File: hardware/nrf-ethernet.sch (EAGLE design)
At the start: 71 parts, among them J2 J0026, J3 RJ45-8PTH, U1 KSZ8081RNA, U2 NRF24L01SMD, U4 MIC5301, U5 MAX3051, U6 STM32F107XX, Y1 8MHz, Y2 16M, Y3 25MHz

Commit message: value update
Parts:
- C29, C30: value 16p -> 18p
- R36: value 120 -> 100k
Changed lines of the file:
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@@
 <part name="GND41" library="supply1" deviceset="GND" device=""/>
 <part name="GND42" library="supply1" deviceset="GND" device=""/>
-<part name="R36" library="rcl" deviceset="R-EU_" device="R0603" value="120"/>
+<part name="R36" library="rcl" deviceset="R-EU_" device="R0603" value="100k"/>
 <part name="GND43" library="supply1" deviceset="GND" device=""/>
 <part name="C34" library="rcl" deviceset="C-EU" device="C0603" value="100n"/>
@@
 <part name="P+9" library="supply1" deviceset="VCC" device=""/>
 <part name="P+12" library="supply1" deviceset="VCC" device=""/>
-<part name="C29" library="rcl" deviceset="C-EU" device="C0603" value="16p"/>
-<part name="C30" library="rcl" deviceset="C-EU" device="C0603" value="16p"/>
+<part name="C29" library="rcl" deviceset="C-EU" device="C0603" value="18p"/>
+<part name="C30" library="rcl" deviceset="C-EU" device="C0603" value="18p"/>
 <part name="C6" library="rcl" deviceset="C-EU" device="C0603" value=".1u"/>
 <part name="C17" library="rcl" deviceset="C-EU" device="C0603" value=".1u"/>

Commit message: hw: fix some part number value
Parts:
- C29, C30: value 18p -> 33p
- Y1: value 8MHz -> 25MHz
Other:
- note removed: "Alternative: 25MHz"
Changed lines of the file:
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@@
 <part name="LED3" library="led" deviceset="LED" device="CHIPLED_0805"/>
 <part name="S3" library="sparkfun" deviceset="SWITCH-MOMENTARY-2" device="SMD" value="SWITCH"/>
-<part name="Y1" library="sparkfun" deviceset="CRYSTAL" device="5X3" value="8MHz"/>
+<part name="Y1" library="sparkfun" deviceset="CRYSTAL" device="5X3" value="25MHz"/>
 <part name="GND6" library="supply1" deviceset="GND" device=""/>
 <part name="GND7" library="supply1" deviceset="GND" device=""/>
@@
 <part name="P+9" library="supply1" deviceset="VCC" device=""/>
 <part name="P+12" library="supply1" deviceset="VCC" device=""/>
-<part name="C29" library="rcl" deviceset="C-EU" device="C0603" value="18p"/>
-<part name="C30" library="rcl" deviceset="C-EU" device="C0603" value="18p"/>
+<part name="C29" library="rcl" deviceset="C-EU" device="C0603" value="33p"/>
+<part name="C30" library="rcl" deviceset="C-EU" device="C0603" value="33p"/>
 <part name="C6" library="rcl" deviceset="C-EU" device="C0603" value=".1u"/>
 <part name="C17" library="rcl" deviceset="C-EU" device="C0603" value=".1u"/>
@@
 <text x="96.52" y="134.62" size="1.778" layer="97">GPIO</text>
 <text x="15.24" y="149.86" size="1.778" layer="97" rot="MR0">GPIO</text>
-<text x="111.76" y="106.68" size="1.778" layer="97">Alternative:
-25MHz</text>
 <text x="15.24" y="147.32" size="1.778" layer="97" rot="MR0">GPIO</text>
 <text x="96.52" y="165.1" size="1.778" layer="97">GPIO</text>
@@
 </schematic>
 </drawing>
-<compatibility>
-<note version="6.3" minversion="6.2.2" severity="warning">
-Since Version 6.2.2 text objects can contain more than one line,
-which will not be processed correctly with this version.
-</note>
-</compatibility>
 </eagle>

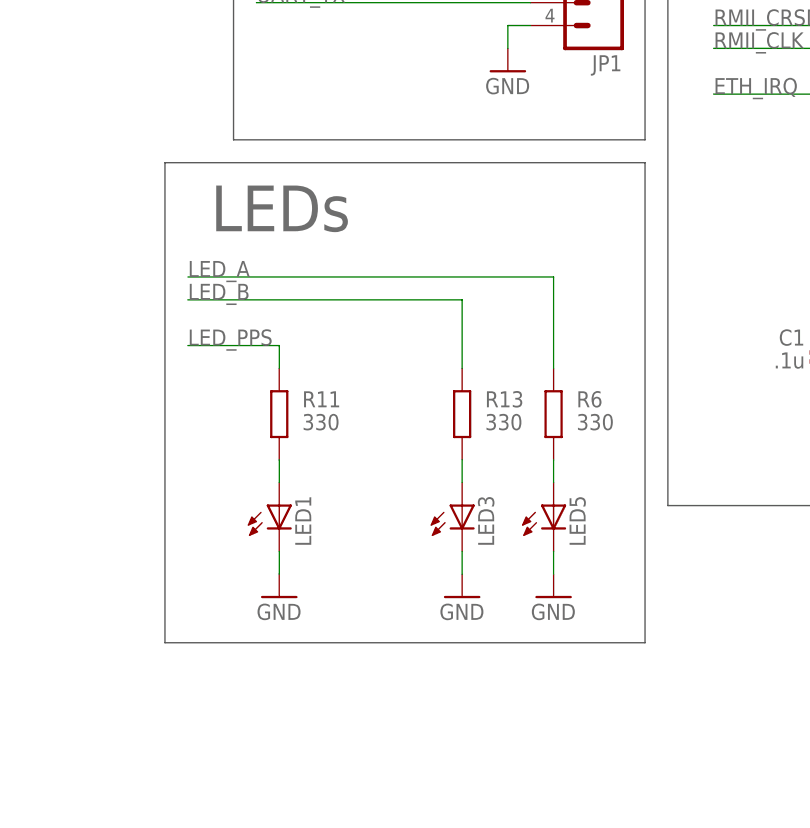
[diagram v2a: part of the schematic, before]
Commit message: hw: mark led colors in schematic
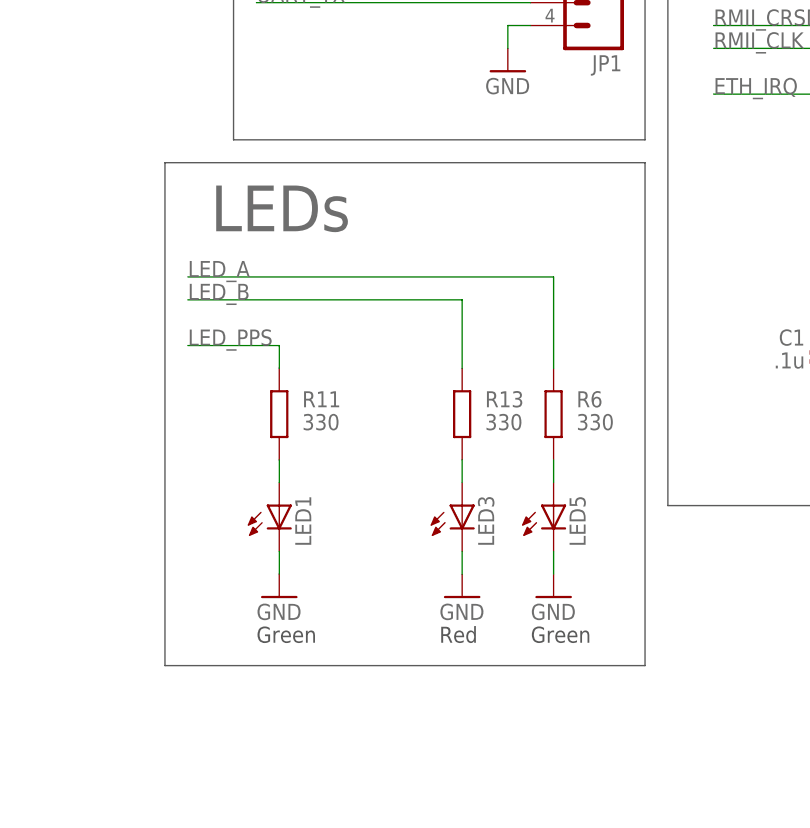
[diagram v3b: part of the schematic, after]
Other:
- note added: "Green"
- note added: "Red"
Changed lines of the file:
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@@
 <wire x1="142.24" y1="215.9" x2="73.66" y2="215.9" width="0.1524" layer="97"/>
 <text x="76.2" y="254" size="5.08" layer="97">LDO</text>
-<wire x1="231.14" y1="66.04" x2="177.8" y2="66.04" width="0.1524" layer="97"/>
+<wire x1="231.14" y1="63.5" x2="177.8" y2="63.5" width="0.1524" layer="97"/>
 <wire x1="231.14" y1="119.38" x2="177.8" y2="119.38" width="0.1524" layer="97"/>
-<wire x1="231.14" y1="119.38" x2="231.14" y2="66.04" width="0.1524" layer="97"/>
-<wire x1="177.8" y1="119.38" x2="177.8" y2="66.04" width="0.1524" layer="97"/>
+<wire x1="231.14" y1="119.38" x2="231.14" y2="63.5" width="0.1524" layer="97"/>
+<wire x1="177.8" y1="119.38" x2="177.8" y2="63.5" width="0.1524" layer="97"/>
 <text x="182.88" y="111.76" size="5.08" layer="95">LEDs</text>
 <wire x1="149.86" y1="58.42" x2="7.62" y2="58.42" width="0.1524" layer="97"/>
@@
 <text x="96.52" y="165.1" size="1.778" layer="97">GPIO</text>
 <text x="96.52" y="129.54" size="1.778" layer="97">GPIO</text>
+<text x="208.28" y="66.04" size="1.778" layer="97">Red</text>
+<text x="218.44" y="66.04" size="1.778" layer="97">Green</text>
+<text x="187.96" y="66.04" size="1.778" layer="97">Green</text>
 </plain>
 <instances>
